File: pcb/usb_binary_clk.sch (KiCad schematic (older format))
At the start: 40 parts, among them J1 USB_B_Micro, J2 USB_B_Micro, SW1 SW_Push, SW2 SW_Push, SW3 SW_Push, U1 MCP7940N-xP, U2 ATtiny84V-10PU, Y1 Crystal

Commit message: Modify pcb layout
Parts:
- J1, J2: symbol Connector:USB_B_Micro -> usb_binary_clk-rescue:USB_B_Micro-Connector
- U2: symbol MCU_Microchip_ATtiny:ATtiny84V-10PU -> usb_binary_clk-rescue:ATtiny84V-10PU-MCU_Microchip_ATtiny
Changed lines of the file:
@@
 EESchema Schematic File Version 4
+LIBS:usb_binary_clk-cache
 EELAYER 30 0
 EELAYER END
@@
 F 3 "~" H 8550 1800 50  0001 C CNN
 	1    8550 1800
-	0    1    1    0
+	0    -1   -1   0
 $EndComp
 $Comp
@@
 $EndComp
 $Comp
-L Connector:USB_B_Micro J2
+L usb_binary_clk-rescue:USB_B_Micro-Connector J2
 U 1 1 60FCFE26
 P 2450 1300
@@
 $EndComp
 $Comp
-L Connector:USB_B_Micro J1
+L usb_binary_clk-rescue:USB_B_Micro-Connector J1
 U 1 1 611ED4E3
 P 1300 1300
@@
 $EndComp
 $Comp
-L MCU_Microchip_ATtiny:ATtiny84V-10PU U2
+L usb_binary_clk-rescue:ATtiny84V-10PU-MCU_Microchip_ATtiny U2
 U 1 1 60FA63B0
 P 8950 4750

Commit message: finalizes part position
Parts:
- BT1: footprint Battery:BatteryHolder_Keystone_3001_1x12mm -> binary_clk_parts:bat-hld-012
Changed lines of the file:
@@
 EESchema Schematic File Version 4
-LIBS:usb_binary_clk-cache
 EELAYER 30 0
 EELAYER END
@@
 F 0 "BT1" H 5118 1896 50  0000 L CNN
 F 1 "Battery_Cell" H 5118 1805 50  0000 L CNN
-F 2 "Battery:BatteryHolder_Keystone_3001_1x12mm" V 5000 1860 50  0001 C CNN
+F 2 "binary_clk_parts:bat-hld-012" V 5000 1860 50  0001 C CNN
 F 3 "~" V 5000 1860 50  0001 C CNN
 	1    5000 1800

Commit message: fix broken schematic symbols
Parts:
- J1, J2: symbol usb_binary_clk-rescue:USB_B_Micro-Connector -> Connector:USB_B_Micro
- U2: symbol usb_binary_clk-rescue:ATtiny84V-10PU-MCU_Microchip_ATtiny -> MCU_Microchip_ATtiny:ATtiny84V-10PU
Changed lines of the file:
@@
 $EndComp
 $Comp
-L usb_binary_clk-rescue:USB_B_Micro-Connector J2
+L Connector:USB_B_Micro J2
 U 1 1 60FCFE26
 P 2450 1300
@@
 $EndComp
 $Comp
-L usb_binary_clk-rescue:USB_B_Micro-Connector J1
+L Connector:USB_B_Micro J1
 U 1 1 611ED4E3
 P 1300 1300
@@
 $EndComp
 $Comp
-L usb_binary_clk-rescue:ATtiny84V-10PU-MCU_Microchip_ATtiny U2
+L MCU_Microchip_ATtiny:ATtiny84V-10PU U2
 U 1 1 60FA63B0
 P 8950 4750

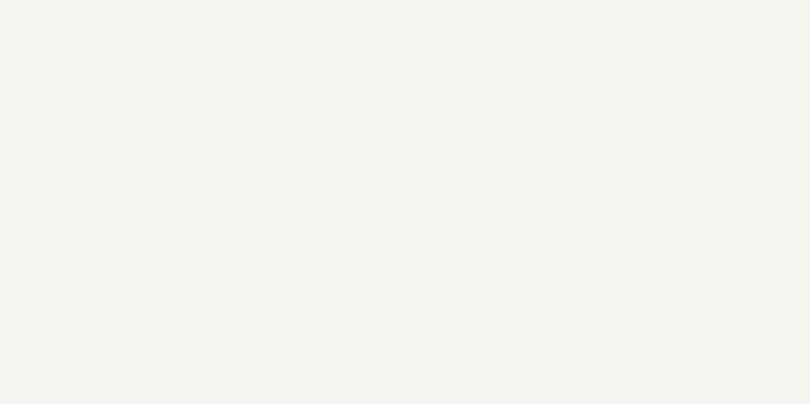
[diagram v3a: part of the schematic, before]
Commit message: change usb port footprints, add programmer pads
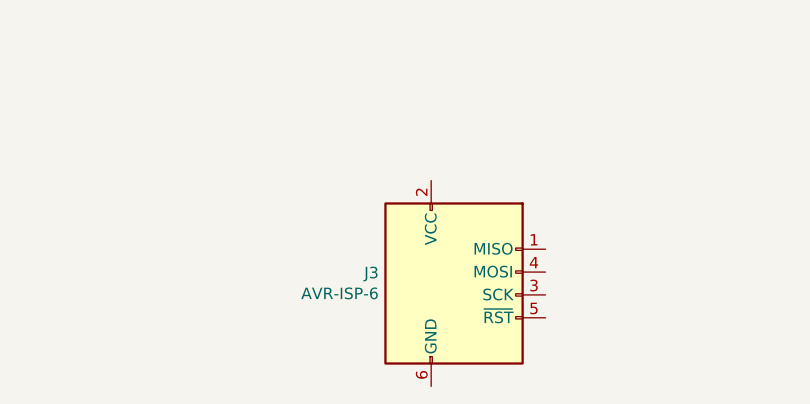
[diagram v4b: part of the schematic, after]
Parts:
- added J3: AVR-ISP-6, binary_clk_parts:isp_pogoPinPads, symbol Connector:AVR-ISP-6
- J1, J2: footprint Connector_USB:USB_Micro-B_GCT_USB3076-30-A -> binary_clk_parts:UJ2MIBHGSMTTR
- R1, R2, R3, R4, R6, R7, R8, R9: footprint Resistor_THT:R_Axial_DIN0204_L3.6mm_D1.6mm_P7.62mm_Horizontal -> Resistor_THT:R_Axial_DIN0207_L6.3mm_D2.5mm_P7.62mm_Horizontal
- R10, R5: footprint Resistor_THT:R_Axial_DIN0204_L3.6mm_D1.6mm_P7.62mm_Horizontal -> Resistor_THT:R_Axial_DIN0207_L6.3mm_D2.5mm_P10.16mm_Horizontal
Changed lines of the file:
@@
 F 0 "J2" H 2507 1767 50  0000 C CNN
 F 1 "USB_B_Micro" H 2507 1676 50  0000 C CNN
-F 2 "Connector_USB:USB_Micro-B_GCT_USB3076-30-A" H 2600 1250 50  0001 C CNN
+F 2 "binary_clk_parts:UJ2MIBHGSMTTR" H 2600 1250 50  0001 C CNN
 F 3 "~" H 2600 1250 50  0001 C CNN
 	1    2450 1300
@@
 F 0 "J1" H 1357 1767 50  0000 C CNN
 F 1 "USB_B_Micro" H 1357 1676 50  0000 C CNN
-F 2 "Connector_USB:USB_Micro-B_GCT_USB3076-30-A" H 1450 1250 50  0001 C CNN
+F 2 "binary_clk_parts:UJ2MIBHGSMTTR" H 1450 1250 50  0001 C CNN
 F 3 "~" H 1450 1250 50  0001 C CNN
 	1    1300 1300
@@
 F 0 "R6" H 2070 3396 50  0000 L CNN
 F 1 "47k" H 2070 3305 50  0000 L CNN
-F 2 "Resistor_THT:R_Axial_DIN0204_L3.6mm_D1.6mm_P7.62mm_Horizontal" V 1930 3350 50  0001 C CNN
+F 2 "Resistor_THT:R_Axial_DIN0207_L6.3mm_D2.5mm_P7.62mm_Horizontal" V 1930 3350 50  0001 C CNN
 F 3 "~" H 2000 3350 50  0001 C CNN
 	1    2000 3350
@@
 F 0 "R9" H 2070 4596 50  0000 L CNN
 F 1 "68k" H 2070 4505 50  0000 L CNN
-F 2 "Resistor_THT:R_Axial_DIN0204_L3.6mm_D1.6mm_P7.62mm_Horizontal" V 1930 4550 50  0001 C CNN
+F 2 "Resistor_THT:R_Axial_DIN0207_L6.3mm_D2.5mm_P7.62mm_Horizontal" V 1930 4550 50  0001 C CNN
 F 3 "~" H 2000 4550 50  0001 C CNN
 	1    2000 4550
@@
 F 0 "R8" H 2070 4196 50  0000 L CNN
 F 1 "24k" H 2070 4105 50  0000 L CNN
-F 2 "Resistor_THT:R_Axial_DIN0204_L3.6mm_D1.6mm_P7.62mm_Horizontal" V 1930 4150 50  0001 C CNN
+F 2 "Resistor_THT:R_Axial_DIN0207_L6.3mm_D2.5mm_P7.62mm_Horizontal" V 1930 4150 50  0001 C CNN
 F 3 "~" H 2000 4150 50  0001 C CNN
 	1    2000 4150
@@
 F 0 "R5" H 10220 4946 50  0000 L CNN
 F 1 "4.7k" H 10220 4855 50  0000 L CNN
-F 2 "Resistor_THT:R_Axial_DIN0204_L3.6mm_D1.6mm_P7.62mm_Horizontal" V 10080 4900 50  0001 C CNN
+F 2 "Resistor_THT:R_Axial_DIN0207_L6.3mm_D2.5mm_P10.16mm_Horizontal" V 10080 4900 50  0001 C CNN
 F 3 "~" H 10150 4900 50  0001 C CNN
 	1    10150 4900
@@
 F 0 "R3" H 10520 4746 50  0000 L CNN
 F 1 "4.7k" H 10520 4655 50  0000 L CNN
-F 2 "Resistor_THT:R_Axial_DIN0204_L3.6mm_D1.6mm_P7.62mm_Horizontal" V 10380 4700 50  0001 C CNN
+F 2 "Resistor_THT:R_Axial_DIN0207_L6.3mm_D2.5mm_P7.62mm_Horizontal" V 10380 4700 50  0001 C CNN
 F 3 "~" H 10450 4700 50  0001 C CNN
 	1    10450 4700
@@
 F 0 "R2" V 6043 3450 50  0000 C CNN
 F 1 "82" V 6134 3450 50  0000 C CNN
-F 2 "Resistor_THT:R_Axial_DIN0204_L3.6mm_D1.6mm_P7.62mm_Horizontal" V 6180 3450 50  0001 C CNN
+F 2 "Resistor_THT:R_Axial_DIN0207_L6.3mm_D2.5mm_P7.62mm_Horizontal" V 6180 3450 50  0001 C CNN
 F 3 "~" H 6250 3450 50  0001 C CNN
 	1    6250 3450
@@
 F 0 "R1" V 6043 2950 50  0000 C CNN
 F 1 "82" V 6134 2950 50  0000 C CNN
-F 2 "Resistor_THT:R_Axial_DIN0204_L3.6mm_D1.6mm_P7.62mm_Horizontal" V 6180 2950 50  0001 C CNN
+F 2 "Resistor_THT:R_Axial_DIN0207_L6.3mm_D2.5mm_P7.62mm_Horizontal" V 6180 2950 50  0001 C CNN
 F 3 "~" H 6250 2950 50  0001 C CNN
 	1    6250 2950
@@
 F 0 "R4" V 6043 3950 50  0000 C CNN
 F 1 "82" V 6134 3950 50  0000 C CNN
-F 2 "Resistor_THT:R_Axial_DIN0204_L3.6mm_D1.6mm_P7.62mm_Horizontal" V 6180 3950 50  0001 C CNN
+F 2 "Resistor_THT:R_Axial_DIN0207_L6.3mm_D2.5mm_P7.62mm_Horizontal" V 6180 3950 50  0001 C CNN
 F 3 "~" H 6250 3950 50  0001 C CNN
 	1    6250 3950
@@
 F 0 "R7" V 6043 4450 50  0000 C CNN
 F 1 "82" V 6134 4450 50  0000 C CNN
-F 2 "Resistor_THT:R_Axial_DIN0204_L3.6mm_D1.6mm_P7.62mm_Horizontal" V 6180 4450 50  0001 C CNN
+F 2 "Resistor_THT:R_Axial_DIN0207_L6.3mm_D2.5mm_P7.62mm_Horizontal" V 6180 4450 50  0001 C CNN
 F 3 "~" H 6250 4450 50  0001 C CNN
 	1    6250 4450
@@
 F 0 "R10" H 1570 6696 50  0000 L CNN
 F 1 "10k" H 1570 6605 50  0000 L CNN
-F 2 "Resistor_THT:R_Axial_DIN0204_L3.6mm_D1.6mm_P7.62mm_Horizontal" V 1430 6650 50  0001 C CNN
+F 2 "Resistor_THT:R_Axial_DIN0207_L6.3mm_D2.5mm_P10.16mm_Horizontal" V 1430 6650 50  0001 C CNN
 F 3 "~" H 1500 6650 50  0001 C CNN
 	1    1500 6650
@@
 Text Label 8100 1700 0    50   ~ 0
 clk-
+$Comp
+L Connector:AVR-ISP-6 J3
+U 1 1 61B50CC1
+P 4200 6850
+F 0 "J3" H 3871 6946 50  0000 R CNN
+F 1 "AVR-ISP-6" H 3871 6855 50  0000 R CNN
+F 2 "binary_clk_parts:isp_pogoPinPads" V 3950 6900 50  0001 C CNN
+F 3 " ~" H 2925 6300 50  0001 C CNN
+	1    4200 6850
+	1    0    0    -1
+$EndComp
 $EndSCHEMATC

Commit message: rearrange footprint references + add icons
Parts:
- renumbered R4 to R3, R7 to R4, R3 to R6, R6 to R7
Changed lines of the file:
@@
 $EndComp
 $Comp
-L Device:R R6
+L Device:R R7
 U 1 1 61255740
 P 2000 3350
-F 0 "R6" H 2070 3396 50  0000 L CNN
+F 0 "R7" H 2070 3396 50  0000 L CNN
 F 1 "47k" H 2070 3305 50  0000 L CNN
 F 2 "Resistor_THT:R_Axial_DIN0207_L6.3mm_D2.5mm_P7.62mm_Horizontal" V 1930 3350 50  0001 C CNN
@@
 $EndComp
 $Comp
-L Device:R R3
+L Device:R R6
 U 1 1 6123AC0B
 P 10450 4700
-F 0 "R3" H 10520 4746 50  0000 L CNN
+F 0 "R6" H 10520 4746 50  0000 L CNN
 F 1 "4.7k" H 10520 4655 50  0000 L CNN
 F 2 "Resistor_THT:R_Axial_DIN0207_L6.3mm_D2.5mm_P7.62mm_Horizontal" V 10380 4700 50  0001 C CNN
@@
 	5400 4900 5650 4900
 $Comp
-L Device:R R4
+L Device:R R3
 U 1 1 6184C834
 P 6250 3950
-F 0 "R4" V 6043 3950 50  0000 C CNN
+F 0 "R3" V 6043 3950 50  0000 C CNN
 F 1 "82" V 6134 3950 50  0000 C CNN
 F 2 "Resistor_THT:R_Axial_DIN0207_L6.3mm_D2.5mm_P7.62mm_Horizontal" V 6180 3950 50  0001 C CNN
@@
 $EndComp
 $Comp
-L Device:R R7
+L Device:R R4
 U 1 1 6184C2B8
 P 6250 4450
-F 0 "R7" V 6043 4450 50  0000 C CNN
+F 0 "R4" V 6043 4450 50  0000 C CNN
 F 1 "82" V 6134 4450 50  0000 C CNN
 F 2 "Resistor_THT:R_Axial_DIN0207_L6.3mm_D2.5mm_P7.62mm_Horizontal" V 6180 4450 50  0001 C CNN

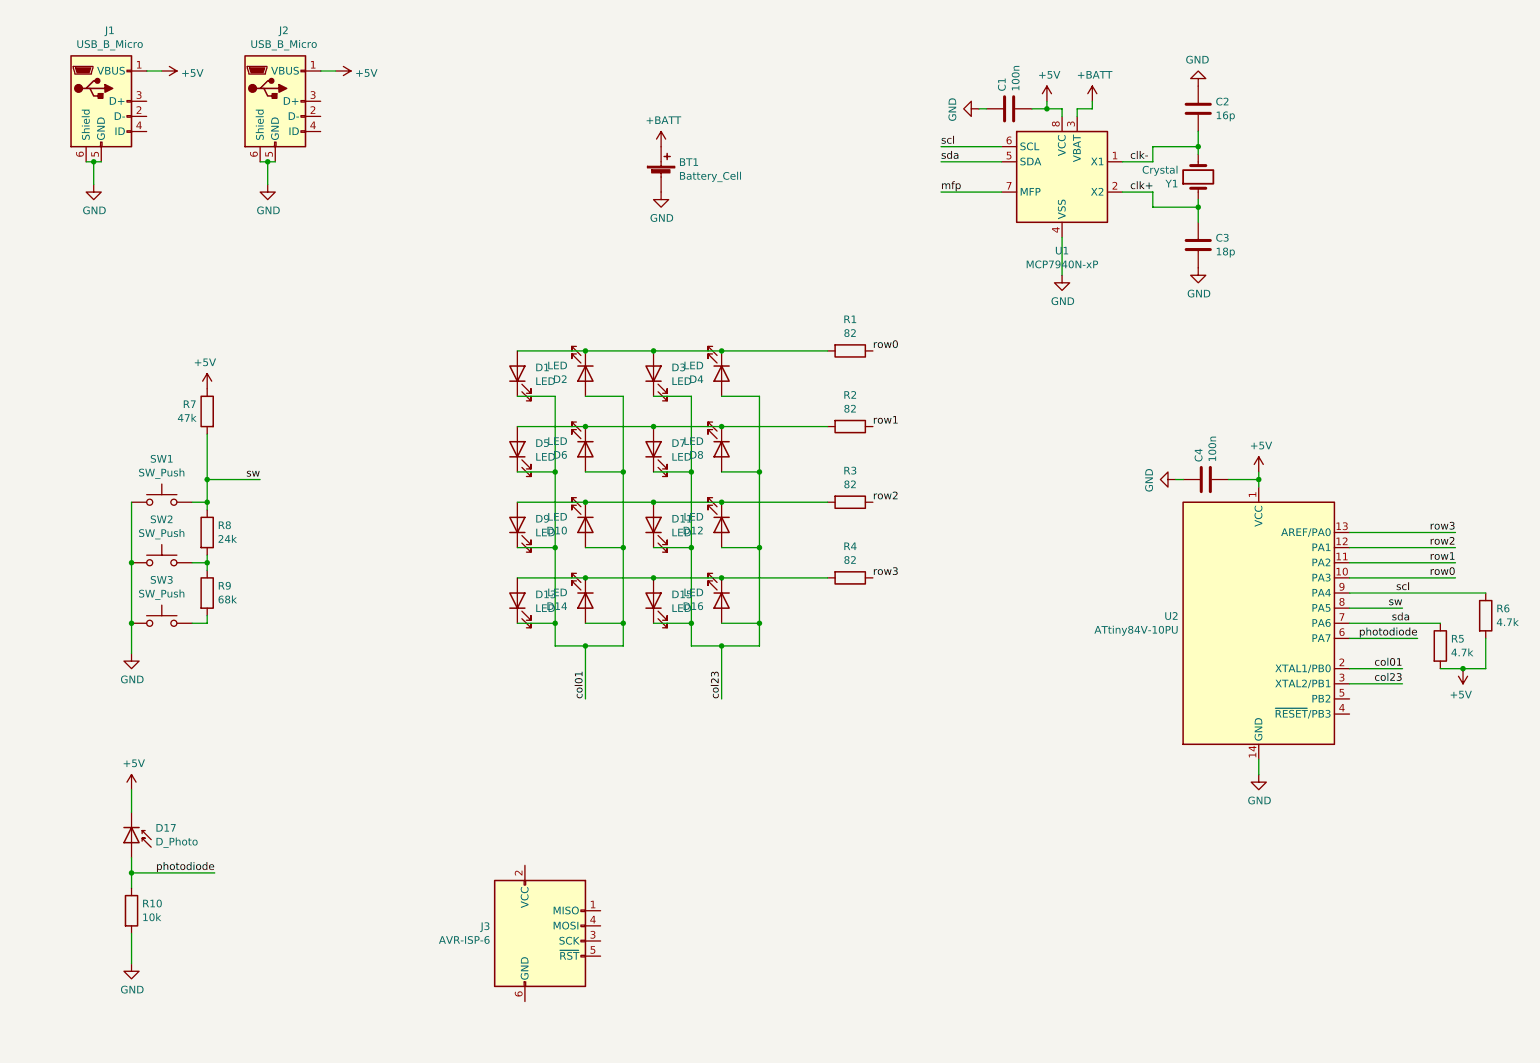
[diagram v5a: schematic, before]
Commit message: connect programmer; add qr code; create gerber files for first order
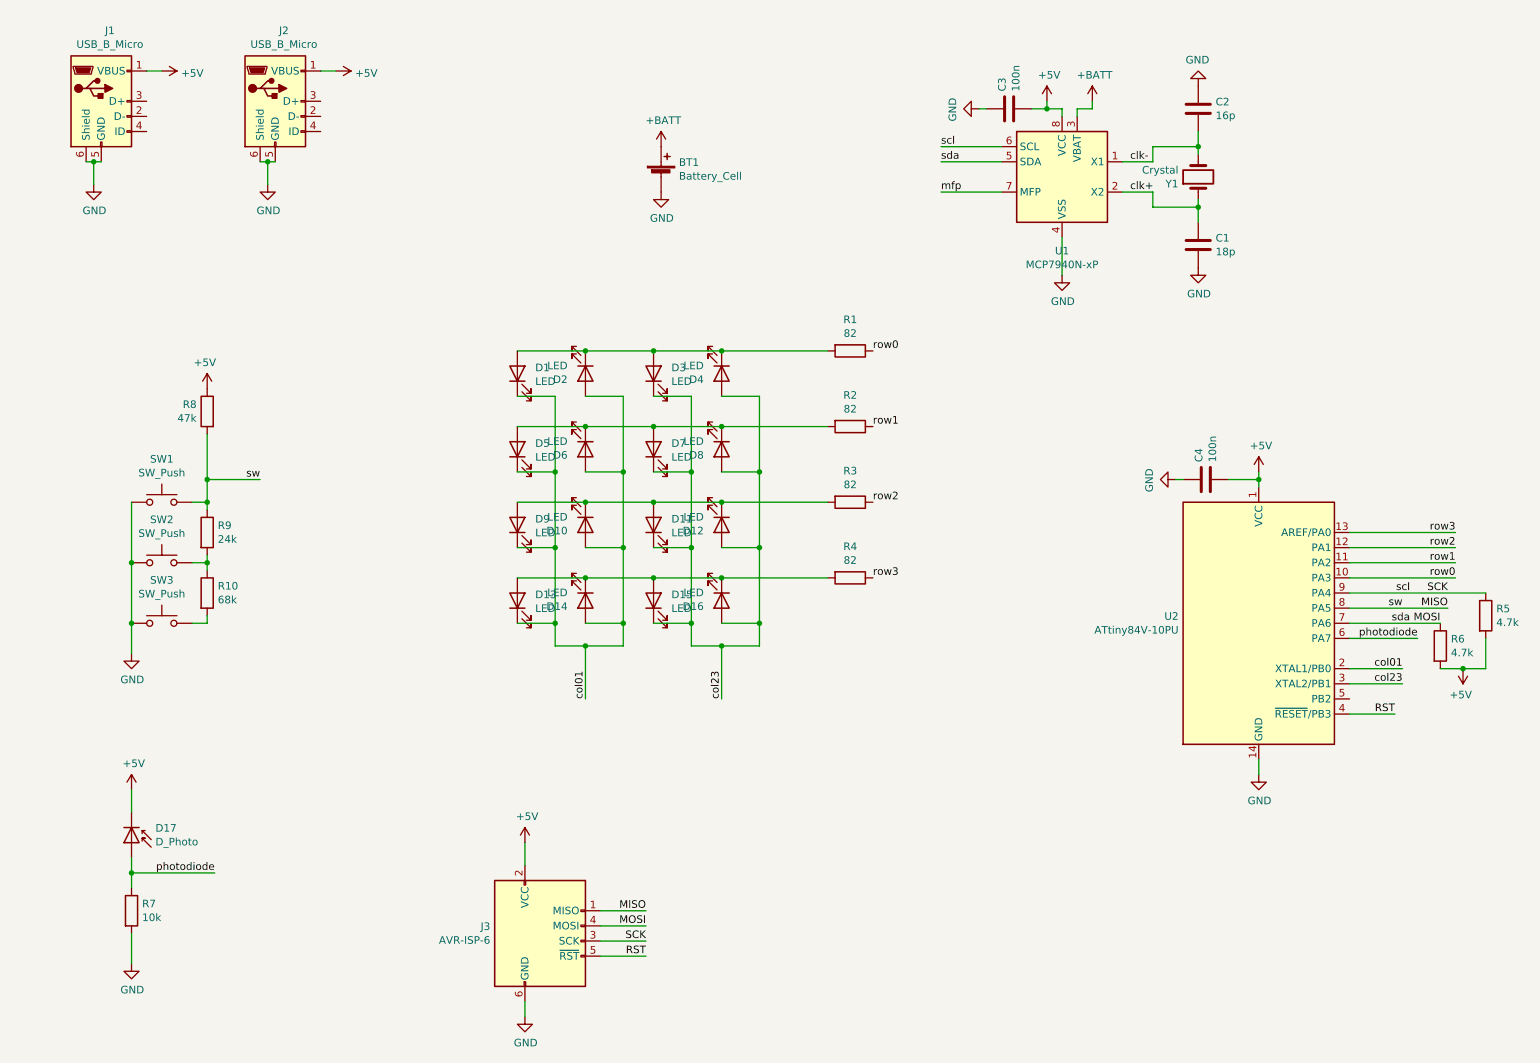
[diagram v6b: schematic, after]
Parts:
- renumbered C3 to C1, C1 to C3, R9 to R10, R6 to R5, R5 to R6, R10 to R7, R7 to R8, R8 to R9
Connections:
- net scl is gone; now on net SCK: R5.1, U1.6 (SCL), U2.9 (PA4)
- net sda is gone; now on net MOSI: R6.1, U1.5 (SDA), U2.7 (PA6)
- net sw is gone; now on net MISO: R8.2, R9.1, SW1.1, U2.8 (PA5)
- net +5V: now also J3.2 (VCC)
- net GND: now also J3.6 (GND)
- net RST: now reaches U2.4 (~RESET~/PB3)
- net RST: now also J3.5 (~RST)
- net MISO: now reaches J3.1 (MISO)
- net SCK: now reaches J3.3 (SCK)
- net MOSI: now reaches J3.4 (MOSI)
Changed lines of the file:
@@
 $EndComp
 $Comp
-L Device:C C3
+L Device:C C1
 U 1 1 60FDC6DB
 P 8550 2250
-F 0 "C3" H 8665 2296 50  0000 L CNN
+F 0 "C1" H 8665 2296 50  0000 L CNN
 F 1 "18p" H 8665 2205 50  0000 L CNN
 F 2 "Capacitor_THT:C_Disc_D4.3mm_W1.9mm_P5.00mm" H 8588 2100 50  0001 C CNN
@@
 $EndComp
 $Comp
-L Device:C C1
+L Device:C C3
 U 1 1 61158066
 P 7300 1350
-F 0 "C1" H 7415 1396 50  0000 L CNN
+F 0 "C3" H 7415 1396 50  0000 L CNN
 F 1 "100n" H 7415 1305 50  0000 L CNN
 F 2 "Capacitor_THT:C_Disc_D4.3mm_W1.9mm_P5.00mm" H 7338 1200 50  0001 C CNN
@@
 $EndComp
 $Comp
-L Device:R R7
+L Device:R R8
 U 1 1 61255740
 P 2000 3350
-F 0 "R7" H 2070 3396 50  0000 L CNN
+F 0 "R8" H 2070 3396 50  0000 L CNN
 F 1 "47k" H 2070 3305 50  0000 L CNN
 F 2 "Resistor_THT:R_Axial_DIN0207_L6.3mm_D2.5mm_P7.62mm_Horizontal" V 1930 3350 50  0001 C CNN
@@
 $EndComp
 $Comp
-L Device:R R9
+L Device:R R10
 U 1 1 60FE618D
 P 2000 4550
-F 0 "R9" H 2070 4596 50  0000 L CNN
+F 0 "R10" H 2070 4596 50  0000 L CNN
 F 1 "68k" H 2070 4505 50  0000 L CNN
 F 2 "Resistor_THT:R_Axial_DIN0207_L6.3mm_D2.5mm_P7.62mm_Horizontal" V 1930 4550 50  0001 C CNN
@@
 $EndComp
 $Comp
-L Device:R R8
+L Device:R R9
 U 1 1 60FE5BF1
 P 2000 4150
-F 0 "R8" H 2070 4196 50  0000 L CNN
+F 0 "R9" H 2070 4196 50  0000 L CNN
 F 1 "24k" H 2070 4105 50  0000 L CNN
 F 2 "Resistor_THT:R_Axial_DIN0207_L6.3mm_D2.5mm_P7.62mm_Horizontal" V 1930 4150 50  0001 C CNN
@@
 $EndComp
 $Comp
-L Device:R R5
+L Device:R R6
 U 1 1 6123D27B
 P 10150 4900
-F 0 "R5" H 10220 4946 50  0000 L CNN
+F 0 "R6" H 10220 4946 50  0000 L CNN
 F 1 "4.7k" H 10220 4855 50  0000 L CNN
 F 2 "Resistor_THT:R_Axial_DIN0207_L6.3mm_D2.5mm_P10.16mm_Horizontal" V 10080 4900 50  0001 C CNN
@@
 $EndComp
 $Comp
-L Device:R R6
+L Device:R R5
 U 1 1 6123AC0B
 P 10450 4700
-F 0 "R6" H 10520 4746 50  0000 L CNN
+F 0 "R5" H 10520 4746 50  0000 L CNN
 F 1 "4.7k" H 10520 4655 50  0000 L CNN
 F 2 "Resistor_THT:R_Axial_DIN0207_L6.3mm_D2.5mm_P7.62mm_Horizontal" V 10380 4700 50  0001 C CNN
@@
 Text Label 9900 4650 2    50   ~ 0
 sw
-Wire Wire Line
-	9900 4650 9550 4650
 Connection ~ 4950 2950
 Connection ~ 4950 3450
@@
 $EndComp
 $Comp
-L Device:R R10
+L Device:R R7
 U 1 1 6183B33F
 P 1500 6650
-F 0 "R10" H 1570 6696 50  0000 L CNN
+F 0 "R7" H 1570 6696 50  0000 L CNN
 F 1 "10k" H 1570 6605 50  0000 L CNN
 F 2 "Resistor_THT:R_Axial_DIN0207_L6.3mm_D2.5mm_P10.16mm_Horizontal" V 1430 6650 50  0001 C CNN
@@
 	1    0    0    -1
 $EndComp
+Text Label 4900 6650 2    50   ~ 0
+MISO
+Text Label 4900 6750 2    50   ~ 0
+MOSI
+Text Label 4900 6850 2    50   ~ 0
+SCK
+Text Label 4900 6950 2    50   ~ 0
+RST
+Wire Wire Line
+	4900 6650 4600 6650
+Wire Wire Line
+	4900 6750 4600 6750
+Wire Wire Line
+	4900 6850 4600 6850
+Wire Wire Line
+	4900 6950 4600 6950
+$Comp
+L power:+5V #PWR?
+U 1 1 61E83871
+P 4100 6200
+F 0 "#PWR?" H 4100 6050 50  0001 C CNN
+F 1 "+5V" H 4115 6373 50  0000 C CNN
+F 2 "" H 4100 6200 50  0001 C CNN
+F 3 "" H 4100 6200 50  0001 C CNN
+	1    4100 6200
+	1    0    0    -1
+$EndComp
+Wire Wire Line
+	4100 6200 4100 6350
+$Comp
+L power:GND #PWR?
+U 1 1 61E8E695
+P 4100 7350
+F 0 "#PWR?" H 4100 7100 50  0001 C CNN
+F 1 "GND" H 4105 7177 50  0000 C CNN
+F 2 "" H 4100 7350 50  0001 C CNN
+F 3 "" H 4100 7350 50  0001 C CNN
+	1    4100 7350
+	1    0    0    -1
+$EndComp
+Wire Wire Line
+	4100 7350 4100 7250
+Text Label 10200 4650 2    50   ~ 0
+MISO
+Wire Wire Line
+	9550 4650 10200 4650
+Text Label 10200 4550 2    50   ~ 0
+SCK
+Text Label 10150 4750 2    50   ~ 0
+MOSI
+Text Label 9850 5350 2    50   ~ 0
+RST
+Wire Wire Line
+	9850 5350 9550 5350
 $EndSCHEMATC
